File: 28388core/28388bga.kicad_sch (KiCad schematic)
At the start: 132 parts, among them IC1 F28388DZWTS, IC2 TPS62420DRCT, IC6 OPA4350EA_250, IC7 TPS3702CX33DDCT, IC8 CDCLVC1104PW, IC9 TPS3702CX12DDCT, J9 Conn_02x07_Odd_Even, Q1 FMMT618TA, Q11 AT24C16C-SSHM-T, Q2 FMMT618TA, Q4 FMMT618TA, Q46 TYPEC-304-ACP16, Q7 FMMT618TA, SW1 SW_DIP_x02, SW2 SW_Push, U1 ADR423ARMZ, Y1 ECS-2520S33-250-FN-TR

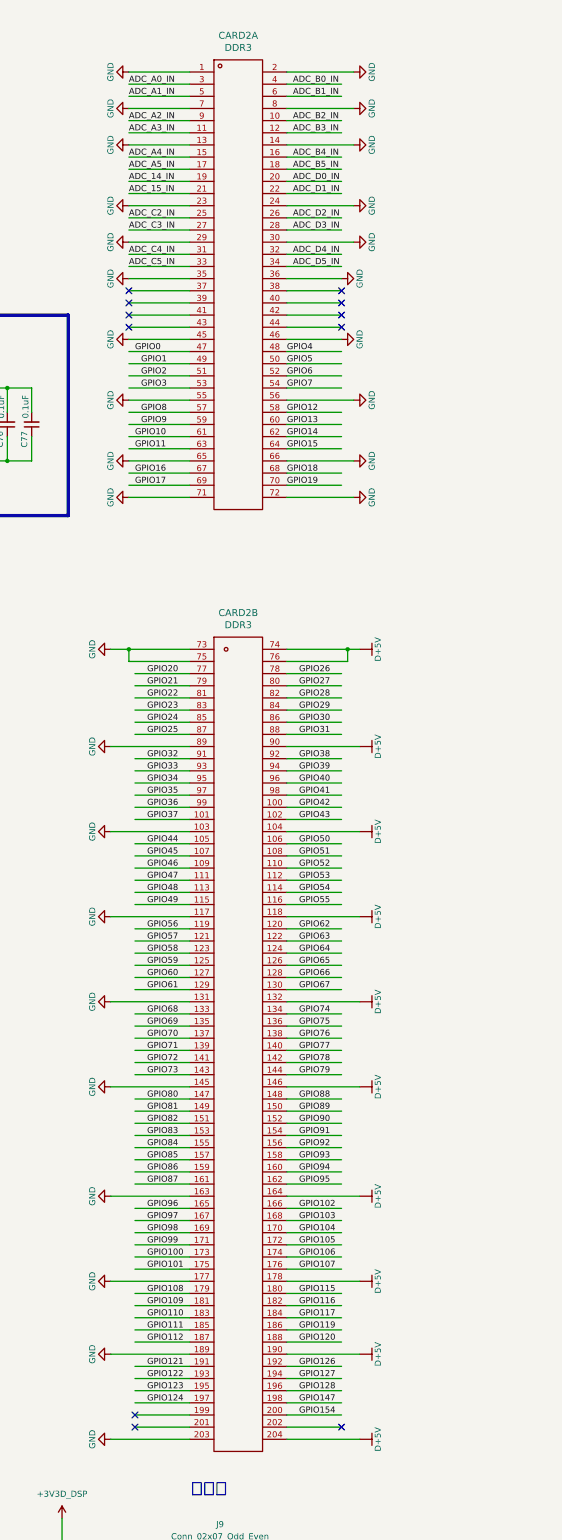
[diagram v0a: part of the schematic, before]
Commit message: 使用100PIN连接器
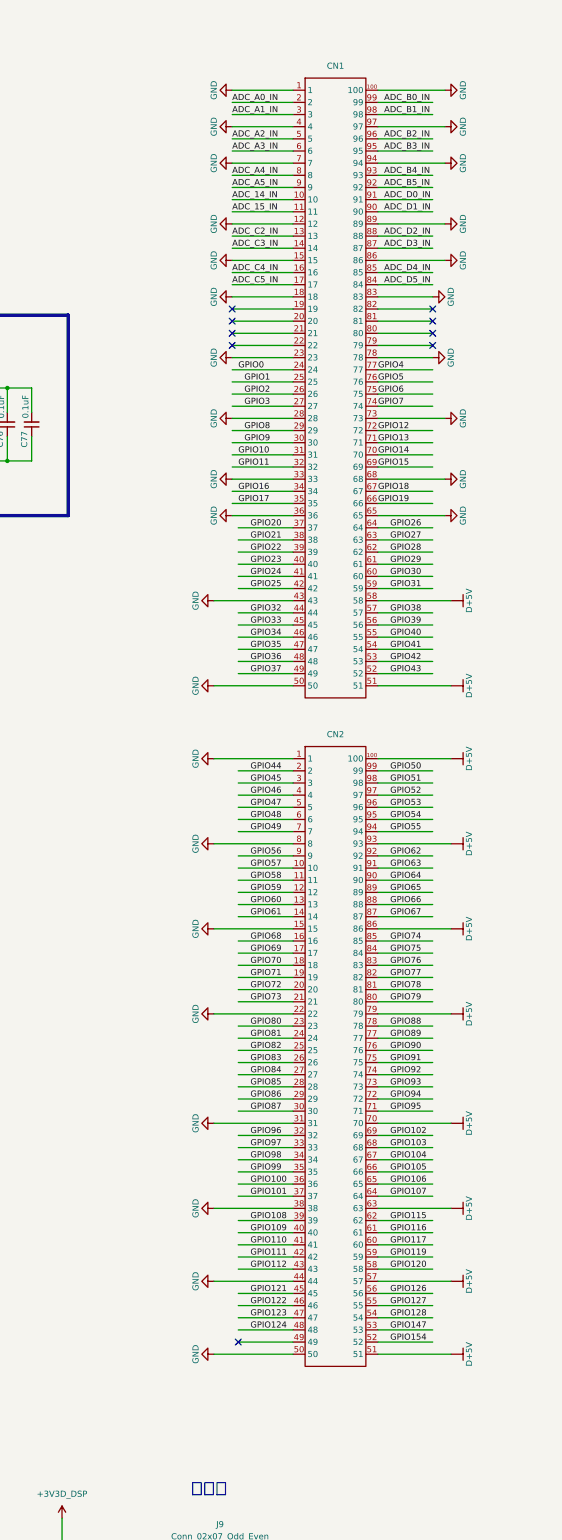
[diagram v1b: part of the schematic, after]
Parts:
- removed CARD2: DDR3, 1mmlab_footprint:PCBComponent_1 - duplicate, symbol 1mmlab:DDR3
- added CN1, CN2: ~, 1mmlab_footprint:CONN-SMD_DF40C-100DS-0.4V-51, symbol 1mmlab:DF40C-100DS-0.4V(51)
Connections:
- net ADC_14_IN: now also CN1.10
- net ADC_15_IN: now also CN1.11
- net ADC_A0_IN: now also CN1.2
- net ADC_A1_IN: now also CN1.3
- net ADC_A2_IN: now also CN1.5
- net ADC_A3_IN: now also CN1.6
- net ADC_A4_IN: now also CN1.8
- net ADC_A5_IN: now also CN1.9
- net ADC_B0_IN: now also CN1.99
- net ADC_B1_IN: now also CN1.98
- net ADC_B2_IN: now also CN1.96
- net ADC_B3_IN: now also CN1.95
- net ADC_B4_IN: now also CN1.93
- net ADC_B5_IN: now also CN1.92
- net ADC_C2_IN: now also CN1.13
- net ADC_C3_IN: now also CN1.14
- net ADC_C4_IN: now also CN1.16
- net ADC_C5_IN: now also CN1.17
- net ADC_D0_IN: now also CN1.91
- net ADC_D1_IN: now also CN1.90
- net ADC_D2_IN: now also CN1.88
- net ADC_D3_IN: now also CN1.87
- net ADC_D4_IN: now also CN1.85
- net ADC_D5_IN: now also CN1.84
- net D+5V: now also CN1.51, CN1.58, CN2.100, CN2.51, CN2.57, CN2.63, CN2.70, CN2.79, CN2.86, CN2.93
- net GND: now also CN1.1, CN1.100, CN1.12, CN1.15, CN1.18, CN1.23, CN1.28, CN1.33, CN1.36, CN1.4, CN1.43, CN1.50, CN1.65, CN1.68, CN1.7, CN1.73, CN1.78, CN1.83, CN1.86, CN1.89, CN1.94, CN1.97, CN2.1, CN2.15, CN2.22, CN2.31, CN2.38, CN2.44, CN2.50, CN2.8
- net GPIO0: now also CN1.24
- net GPIO1: now also CN1.25
- net GPIO10: now also CN1.31
- net GPIO100: now also CN2.36
- net GPIO101: now also CN2.37
- net GPIO102: now also CN2.69
- net GPIO103: now also CN2.68
- net GPIO104: now also CN2.67
- net GPIO105: now also CN2.66
- net GPIO106: now also CN2.65
- net GPIO107: now also CN2.64
- net GPIO108: now also CN2.39
- net GPIO109: now also CN2.40
- net GPIO11: now also CN1.32
- net GPIO110: now also CN2.41
- net GPIO111: now also CN2.42
- net GPIO112: now also CN2.43
- net GPIO115: now also CN2.62
- net GPIO116: now also CN2.61
- net GPIO117: now also CN2.60
- net GPIO119: now also CN2.59
- net GPIO12: now also CN1.72
- net GPIO120: now also CN2.58
- net GPIO121: now also CN2.45
- net GPIO122: now also CN2.46
- net GPIO123: now also CN2.47
- net GPIO124: now also CN2.48
- net GPIO126: now also CN2.56
- net GPIO127: now also CN2.55
- net GPIO128: now also CN2.54
- net GPIO13: now also CN1.71
- net GPIO14: now also CN1.70
- net GPIO147: now also CN2.53
- net GPIO15: now also CN1.69
- net GPIO154: now also CN2.52
- net GPIO16: now also CN1.34
- net GPIO17: now also CN1.35
- net GPIO18: now also CN1.67
- net GPIO19: now also CN1.66
- net GPIO2: now also CN1.26
- net GPIO20: now also CN1.37
- net GPIO21: now also CN1.38
- net GPIO22: now also CN1.39
- net GPIO23: now also CN1.40
- net GPIO24: now also CN1.41
- net GPIO25: now also CN1.42
- net GPIO26: now also CN1.64
- net GPIO27: now also CN1.63
- net GPIO28: now also CN1.62
- net GPIO29: now also CN1.61
- net GPIO3: now also CN1.27
- net GPIO30: now also CN1.60
- net GPIO31: now also CN1.59
- net GPIO32: now also CN1.44
- net GPIO33: now also CN1.45
- net GPIO34: now also CN1.46
- net GPIO35: now also CN1.47
- net GPIO36: now also CN1.48
- net GPIO37: now also CN1.49
- net GPIO38: now also CN1.57
- net GPIO39: now also CN1.56
- net GPIO4: now also CN1.77
- net GPIO40: now also CN1.55
- net GPIO41: now also CN1.54
- net GPIO42: now also CN1.53
- net GPIO43: now also CN1.52
- net GPIO44: now also CN2.2
- net GPIO45: now also CN2.3
- net GPIO46: now also CN2.4
- net GPIO47: now also CN2.5
- net GPIO48: now also CN2.6
- net GPIO49: now also CN2.7
- net GPIO5: now also CN1.76
- net GPIO50: now also CN2.99
- net GPIO51: now also CN2.98
- net GPIO52: now also CN2.97
- net GPIO53: now also CN2.96
- net GPIO54: now also CN2.95
- net GPIO55: now also CN2.94
- net GPIO56: now also CN2.9
- net GPIO57: now also CN2.10
- net GPIO58: now also CN2.11
- net GPIO59: now also CN2.12
- net GPIO6: now also CN1.75
- net GPIO60: now also CN2.13
- net GPIO61: now also CN2.14
- net GPIO62: now also CN2.92
- net GPIO63: now also CN2.91
- net GPIO64: now also CN2.90
- net GPIO65: now also CN2.89
- net GPIO66: now also CN2.88
- net GPIO67: now also CN2.87
- net GPIO68: now also CN2.16
- net GPIO69: now also CN2.17
- net GPIO7: now also CN1.74
- net GPIO70: now also CN2.18
- net GPIO71: now also CN2.19
- net GPIO72: now also CN2.20
- net GPIO73: now also CN2.21
- net GPIO74: now also CN2.85
- net GPIO75: now also CN2.84
- net GPIO76: now also CN2.83
- net GPIO77: now also CN2.82
- net GPIO78: now also CN2.81
- net GPIO79: now also CN2.80
- net GPIO8: now also CN1.29
- net GPIO80: now also CN2.23
- net GPIO81: now also CN2.24
- net GPIO82: now also CN2.25
- net GPIO83: now also CN2.26
- net GPIO84: now also CN2.27
- net GPIO85: now also CN2.28
- net GPIO86: now also CN2.29
- net GPIO87: now also CN2.30
- net GPIO88: now also CN2.78
- net GPIO89: now also CN2.77
- net GPIO9: now also CN1.30
- net GPIO90: now also CN2.76
- net GPIO91: now also CN2.75
- net GPIO92: now also CN2.74
- net GPIO93: now also CN2.73
- net GPIO94: now also CN2.72
- net GPIO95: now also CN2.71
- net GPIO96: now also CN2.32
- net GPIO97: now also CN2.33
- net GPIO98: now also CN2.34
- net GPIO99: now also CN2.35
- no-connect marks 27 -> 25

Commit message: 分组初步
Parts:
- removed CN1, CN2: ~, 1mmlab_footprint:CONN-SMD_DF40C-100DS-0.4V-51, symbol 1mmlab:DF40C-100DS-0.4V(51)
- added CN4: ~, 1mmlab_footprint:CONN-SMD_200P-P0.50_X0510WVS-200AS-LPV01, symbol 1mmlab:X0510WVS-200AS-LPV01
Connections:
- net ADC_14_IN: now also CN4.19
- net ADC_15_IN: now also CN4.21
- net ADC_A0_IN: now also CN4.3
- net ADC_A1_IN: now also CN4.5
- net ADC_A2_IN: now also CN4.9
- net ADC_A3_IN: now also CN4.11
- net ADC_A4_IN: now also CN4.15
- net ADC_A5_IN: now also CN4.17
- net ADC_B0_IN: now also CN4.4
- net ADC_B1_IN: now also CN4.6
- net ADC_B2_IN: now also CN4.10
- net ADC_B3_IN: now also CN4.12
- net ADC_B4_IN: now also CN4.16
- net ADC_B5_IN: now also CN4.18
- net ADC_C2_IN: now also CN4.25
- net ADC_C3_IN: now also CN4.27
- net ADC_C4_IN: now also CN4.31
- net ADC_C5_IN: now also CN4.33
- net ADC_D0_IN: now also CN4.20
- net ADC_D1_IN: now also CN4.22
- net ADC_D2_IN: now also CN4.26
- net ADC_D3_IN: now also CN4.28
- net ADC_D4_IN: now also CN4.32
- net ADC_D5_IN: now also CN4.34
- net GND: now also CN4.1, CN4.13, CN4.14, CN4.2, CN4.23, CN4.24, CN4.29, CN4.30, CN4.35, CN4.36, CN4.45, CN4.46, CN4.7, CN4.8
- net PE_GND: now also CN4.201, CN4.202
- no-connect marks 25 -> 24

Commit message: 分组后分配引脚
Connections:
- net D+5V: now also CN4.106, CN4.128, CN4.146, CN4.162, CN4.172, CN4.188, CN4.200, CN4.90, CN4.98
- net GND: now also CN4.105, CN4.127, CN4.145, CN4.161, CN4.171, CN4.187, CN4.199, CN4.57, CN4.58, CN4.71, CN4.72, CN4.79, CN4.80, CN4.89, CN4.97
- net GPIO0: now also CN4.47
- net GPIO1: now also CN4.49
- net GPIO10: now also CN4.59
- net GPIO100: now also CN4.167
- net GPIO101: now also CN4.169
- net GPIO102: now also CN4.164
- net GPIO103: now also CN4.166
- net GPIO104: now also CN4.168
- net GPIO105: now also CN4.170
- net GPIO106: now also CN4.173
- net GPIO107: now also CN4.175
- net GPIO108: now also CN4.177
- net GPIO109: now also CN4.179
- net GPIO11: now also CN4.61
- net GPIO110: now also CN4.174
- net GPIO111: now also CN4.176
- net GPIO112: now also CN4.178
- net GPIO115: now also CN4.189
- net GPIO116: now also CN4.191
- net GPIO117: now also CN4.193
- net GPIO119: now also CN4.190
- net GPIO120: now also CN4.192
- net GPIO121: now also CN4.181
- net GPIO122: now also CN4.183
- net GPIO123: now also CN4.185
- net GPIO124: now also CN4.180
- net GPIO126: now also CN4.182
- net GPIO127: now also CN4.184
- net GPIO128: now also CN4.186
- net GPIO133: now also CN4.194
- net GPIO147: now also CN4.195
- net GPIO154: now also CN4.196
- net GPIO16: now also CN4.60
- net GPIO17: now also CN4.62
- net GPIO18: now also CN4.64
- net GPIO19: now also CN4.66
- net GPIO2: now also CN4.51
- net GPIO20: now also CN4.68
- net GPIO21: now also CN4.70
- net GPIO22: now also CN4.73
- net GPIO23: now also CN4.75
- net GPIO24: now also CN4.77
- net GPIO25: now also CN4.74
- net GPIO26: now also CN4.76
- net GPIO27: now also CN4.78
- net GPIO28: now also CN4.81
- net GPIO29: now also CN4.83
- net GPIO3: now also CN4.53
- net GPIO30: now also CN4.85
- net GPIO31: now also CN4.87
- net GPIO32: now also CN4.82
- net GPIO33: now also CN4.84
- net GPIO34: now also CN4.86
- net GPIO35: now also CN4.88
- net GPIO36: now also CN4.91
- net GPIO37: now also CN4.93
- net GPIO38: now also CN4.95
- net GPIO39: now also CN4.92
- net GPIO4: now also CN4.48
- net GPIO40: now also CN4.94
- net GPIO41: now also CN4.96
- net GPIO42: now also CN4.100
- net GPIO43: now also CN4.102
- net GPIO44: now also CN4.99
- net GPIO45: now also CN4.101
- net GPIO46: now also CN4.104
- net GPIO47: now also CN4.103
- net GPIO48: now also CN4.107
- net GPIO49: now also CN4.109
- net GPIO5: now also CN4.50
- net GPIO50: now also CN4.111
- net GPIO51: now also CN4.113
- net GPIO52: now also CN4.115
- net GPIO53: now also CN4.117
- net GPIO54: now also CN4.119
- net GPIO55: now also CN4.121
- net GPIO56: now also CN4.123
- net GPIO57: now also CN4.125
- net GPIO58: now also CN4.108
- net GPIO59: now also CN4.110
- net GPIO6: now also CN4.52
- net GPIO60: now also CN4.112
- net GPIO61: now also CN4.114
- net GPIO62: now also CN4.116
- net GPIO63: now also CN4.118
- net GPIO64: now also CN4.120
- net GPIO65: now also CN4.122
- net GPIO66: now also CN4.124
- net GPIO67: now also CN4.126
- net GPIO68: now also CN4.129
- net GPIO69: now also CN4.131
- net GPIO7: now also CN4.54
- net GPIO70: now also CN4.133
- net GPIO71: now also CN4.135
- net GPIO72: now also CN4.137
- net GPIO73: now also CN4.139
- net GPIO74: now also CN4.141
- net GPIO75: now also CN4.143
- net GPIO76: now also CN4.130
- net GPIO77: now also CN4.132
- net GPIO78: now also CN4.134
- net GPIO79: now also CN4.136
- net GPIO8: now also CN4.55
- net GPIO80: now also CN4.138
- net GPIO81: now also CN4.140
- net GPIO82: now also CN4.142
- net GPIO83: now also CN4.144
- net GPIO84: now also CN4.147
- net GPIO85: now also CN4.149
- net GPIO86: now also CN4.148
- net GPIO87: now also CN4.150
- net GPIO88: now also CN4.151
- net GPIO89: now also CN4.153
- net GPIO9: now also CN4.56
- net GPIO90: now also CN4.155
- net GPIO91: now also CN4.157
- net GPIO92: now also CN4.159
- net GPIO93: now also CN4.152
- net GPIO94: now also CN4.154
- net GPIO95: now also CN4.156
- net GPIO96: now also CN4.158
- net GPIO97: now also CN4.160
- net GPIO98: now also CN4.163
- net GPIO99: now also CN4.165
- no-connect marks 24 -> 26
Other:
- moved on the sheet: CN4
